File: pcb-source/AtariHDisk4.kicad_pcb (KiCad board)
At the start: 4 copper layers, 97.3 x 69.6 mm, 78 parts, among them J1 JTAG, J10 ST ACSI BUS, J14 MicroSD Card 0, J2 Program_enable, J3 SD Card 1, J4 UPDI, J5 Conn_01x02_Female, J6 Conn_02x03_Odd_Even, Q3 BC847, Q4 BC847, U1 74LVC245, U11 74LVC8T245, U2 MAX3232, U3 AZ1117-5.0, U4 Oscillator7x5, U5 MCP795xx, U7 AMS1117-3.3, U8 AMS1117-1.8, U9 5M80Z, Y1 32KHz

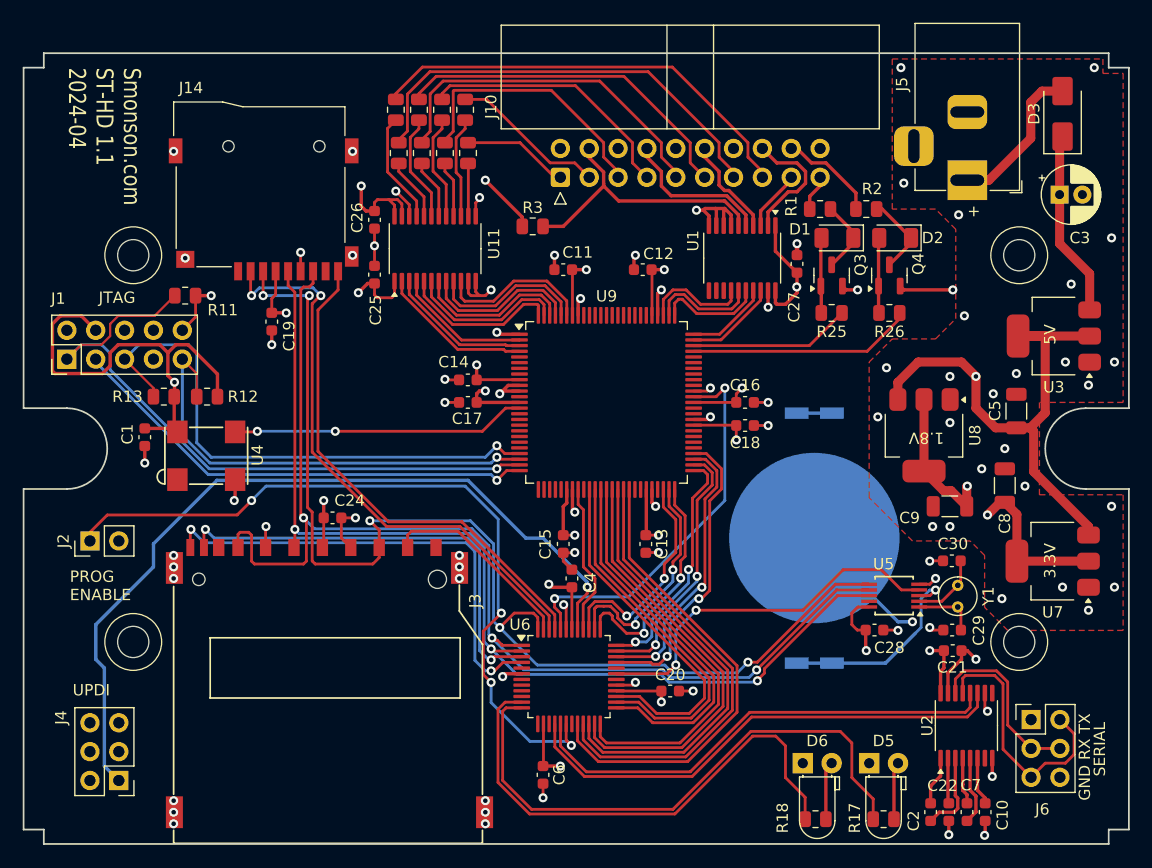
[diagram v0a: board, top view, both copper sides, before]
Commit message: STM32C01 version, now in a working state (#6)
Code for V2 board, proven and now working.
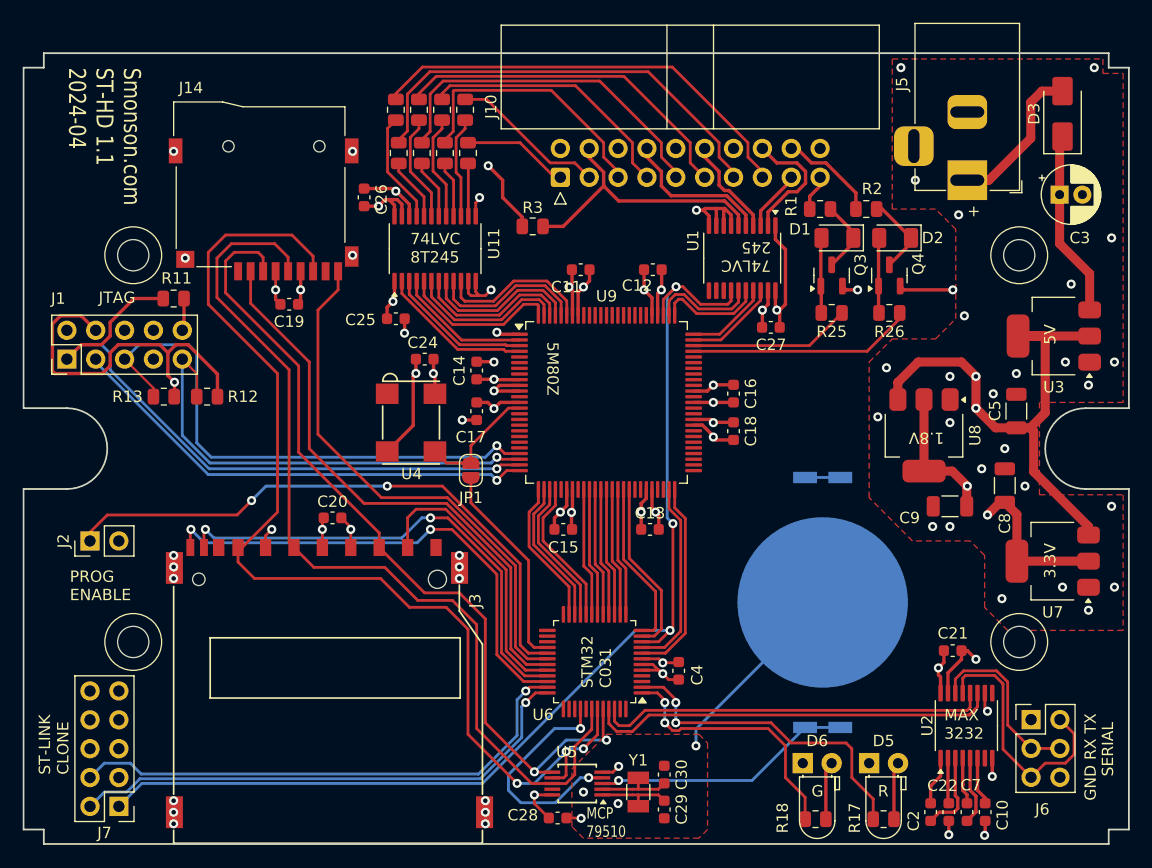
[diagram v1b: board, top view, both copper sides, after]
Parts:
- removed C1, C6: 0.1uF, Capacitor_SMD:C_0603_1608Metric
- removed J4: UPDI, Connector_PinHeader_2.54mm:PinHeader_2x03_P2.54mm_Vertical
- added J7: ST-LINK, Connector_PinHeader_2.54mm:PinHeader_2x05_P2.54mm_Vertical, F.Cu at (63.3, 125.5)
- added JP1: SolderJumper_2_Open, Jumper:SolderJumper-2_P1.3mm_Open_RoundedPad1.0x1.5mm, F.Cu at (94.2, 95.9)
- C21, C28: value C -> 0.1uF
- R17, R18: value 2K -> 220
- R25, R26: value R -> 1K
- U6: value ~ -> STM32C031CxT
- Y1: footprint Crystal:Crystal_C38-LF_D3.0mm_L8.0mm_Vertical -> simon:Crystal_SMD_ECX_31B-2Pin_3.2x1.5mm
- moved Y1 33.5 mm to (109.0, 124.2), turned to 90 degrees
- moved C20 33.4 mm to (82.1, 100.1)
- moved C28 32.4 mm to (101.9, 126.5)
- moved U5 32.4 mm to (103.6, 123.5)
- moved C30 31.5 mm to (111.3, 122.7), turned to 90 degrees
- moved C29 29.9 mm to (111.3, 125.7), turned to -90 degrees
- moved U4 18.0 mm to (88.8, 91.8), turned to 90 degrees
- moved C24 16.2 mm to (90.2, 86.1), turned to 180 degrees
- moved C4 12.4 mm to (112.5, 113.5)
- moved C27 6.04 mm to (120.6, 83.3), turned to 180 degrees
- moved BT1 5.71 mm to (125.2, 107.5)
- moved C25 4.31 mm to (87.6, 82.5), turned to 0 degrees
- moved U6 2.61 mm to (105.1, 112.7), turned to 180 degrees
- moved C26 2.18 mm to (84.8, 71.9), turned to 90 degrees
- moved C19 2.16 mm to (78.2, 81.3), turned to 0 degrees
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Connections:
- R17 pad 1: /ATMega/LED0 -> /Microcontroller/LED0
- R18 pad 1: /ATMega/LED1 -> /Microcontroller/LED1
- U2 pad 11: /ATMega/TX -> /Microcontroller/TX
- U2 pad 12: /ATMega/RX -> /Microcontroller/RX
- U5 pad 4: /ATMega/CLK_SS -> /Microcontroller/CLK_SS
- U6 pad 1: /MISO -> /Microcontroller/LED1
- U6 pad 10: unconnected-(U6-PC0-Pad10) -> /F_RESET
- U6 pad 11: /ATMega/LED1 -> /A_D0
- U6 pad 12: /ATMega/LED0 -> /A_D1
- U6 pad 13: unconnected-(U6-PC3-Pad13) -> /A_D2
- U6 pad 14: +3V3 -> /A_D3
- U6 pad 15: (no net) -> /A_D4
- U6 pad 16: /ATMega/TX -> /A_D5
- U6 pad 17: /ATMega/RX -> /A_D6
- U6 pad 18: Net-(J2-Pin_1) -> /A_D7
- U6 pad 19: unconnected-(U6-PC7-Pad19) -> /A_CS
- U6 pad 2: /SCK -> /Microcontroller/LED0
- U6 pad 20: /A_D0 -> /A_BUS_DIR
- U6 pad 21: /A_D1 -> /A_CMD
- U6 pad 22: /A_D2 -> /A_EXTRA2
- U6 pad 23: /A_D3 -> /A_EXTRA
- U6 pad 24: /A_D4 -> unconnected-(U6-PB12-Pad24)
- U6 pad 25: /A_D5 -> unconnected-(U6-PB13-Pad25)
- U6 pad 26: /A_D6 -> unconnected-(U6-PB14-Pad26)
- U6 pad 27: /A_D7 -> unconnected-(U6-PB15-Pad27)
- U6 pad 28: +3V3 -> /A_CLKOUT
- U6 pad 29: GND -> Net-(J2-Pin_1)
- U6 pad 3: /CARD1_DET -> unconnected-(U6-PC15-Pad3)
- U6 pad 30: unconnected-(U6-PE0-Pad30) -> /CARD0_DET
- U6 pad 31: /ATMega/CLK_SS -> /AVR_SS0
- U6 pad 32: unconnected-(U6-PE2-Pad32) -> /AVR_SS1
- U6 pad 33: /A_EXTRA2 -> /CARD1_DET
- U6 pad 34: /A_EXTRA -> /CARD1_WP
- U6 pad 35: /A_READY -> /Microcontroller/SWDIO
- U6 pad 36: /A_INT -> /Microcontroller/SWCLK
- U6 pad 37: /A_CMD -> unconnected-(U6-PA15-Pad37)
- U6 pad 38: /A_BUS_DIR -> unconnected-(U6-PD0-Pad38)
- U6 pad 39: /A_CS -> unconnected-(U6-PD1-Pad39)
- U6 pad 4: /CARD1_WP -> unconnected-(U6-PF3-Pad4)
- U6 pad 40: /A_RESET -> /Microcontroller/CLK_SS
- U6 pad 41: /ATMega/UPDI -> (no net)
- U6 pad 42: +3V3 -> /SCK
- U6 pad 43: GND -> /MISO
- U6 pad 44: /CLOCK8 -> /MOSI
- U6 pad 45: /CARD0_DET -> /Microcontroller/TX
- U6 pad 46: /AVR_SS0 -> /Microcontroller/RX
- U6 pad 47: /AVR_SS1 -> unconnected-(U6-PB8-Pad47)
- U6 pad 48: /MOSI -> unconnected-(U6-PB9-Pad48)
- U6 pad 5: unconnected-(U6-PB1-Pad5) -> +3V3
- U6 pad 6: GND -> +3V3
- U6 pad 7: unconnected-(U6-PB3-Pad7) -> GND
- U6 pad 8: unconnected-(U6-PB4-Pad8) -> /A_READY
- U6 pad 9: unconnected-(U6-PB5-Pad9) -> /A_INT
- U9 pad 26: unconnected-(U9-IO-Pad26) -> /A_EXTRA
- U9 pad 27: unconnected-(U9-IO-Pad27) -> /A_EXTRA2
- U9 pad 28: unconnected-(U9-IO-Pad28) -> /A_CMD
- U9 pad 29: unconnected-(U9-IO-Pad29) -> /A_BUS_DIR
- U9 pad 33: /A_RESET -> unconnected-(U9-IO-Pad33)
- U9 pad 34: unconnected-(U9-IO-Pad34) -> /A_CS
- U9 pad 48: /A_CS -> unconnected-(U9-IO-Pad48)
- U9 pad 49: /A_BUS_DIR -> /A_INT
- U9 pad 50: /A_CMD -> /A_READY
- U9 pad 51: /A_INT -> unconnected-(U9-IO-Pad51)
- U9 pad 52: /A_READY -> unconnected-(U9-IO-Pad52)
- U9 pad 53: /A_EXTRA -> unconnected-(U9-IO-Pad53)
- U9 pad 54: /A_EXTRA2 -> unconnected-(U9-IO-Pad54)
- U9 pad 64: /CLOCK8 -> unconnected-(U9-IO/CLK3-Pad64)
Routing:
- net +3V3: track 449.2 -> 109.1 mm, vias 17 -> 16
- net /F_RESET: track 9.27 -> 98.2 mm, vias 0 -> 3
- net /ATMega/UPDI: track 72.5 -> 0.00 mm, vias 1 -> 0
- net /ATMega/LED0: track 50.4 -> 0.00 mm
- net /Microcontroller/SWDIO: track 0.00 -> 46.2 mm, vias 0 -> 1
- net /Microcontroller/SWCLK: track 0.00 -> 46.0 mm, vias 0 -> 1
- net /ATMega/LED1: track 45.6 -> 0.00 mm
- net /ATMega/TX: track 44.0 -> 0.00 mm
- net /ATMega/RX: track 42.6 -> 0.00 mm
- net /Microcontroller/TX: track 0.00 -> 36.1 mm
- net /Microcontroller/RX: track 0.00 -> 34.5 mm
- net /CLOCK8: track 34.5 -> 0.00 mm, vias 2 -> 0
- net /ATMega/CLK_SS: track 33.0 -> 0.00 mm, vias 2 -> 0
- net /Microcontroller/LED0: track 0.00 -> 28.9 mm, vias 0 -> 2
- net /A_D2: track 38.9 -> 11.3 mm
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- added copper zone on In2.Cu, net +3V3
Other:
- board text added: "5M80Z"
- board text added: "74LVC 245"
- board text added: "74LVC 8T245"
- board text added: "CR2016"
- board text added: "G"
- board text added: "MAX 3232"
- board text added: "MCP 79510"
- board text added: "R"
- board text added: "ST-LINK CLONE"
- board text added: "STM32 C031"
- board text removed: "UPDI"

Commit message: 1.2 version with 2 SPI buses
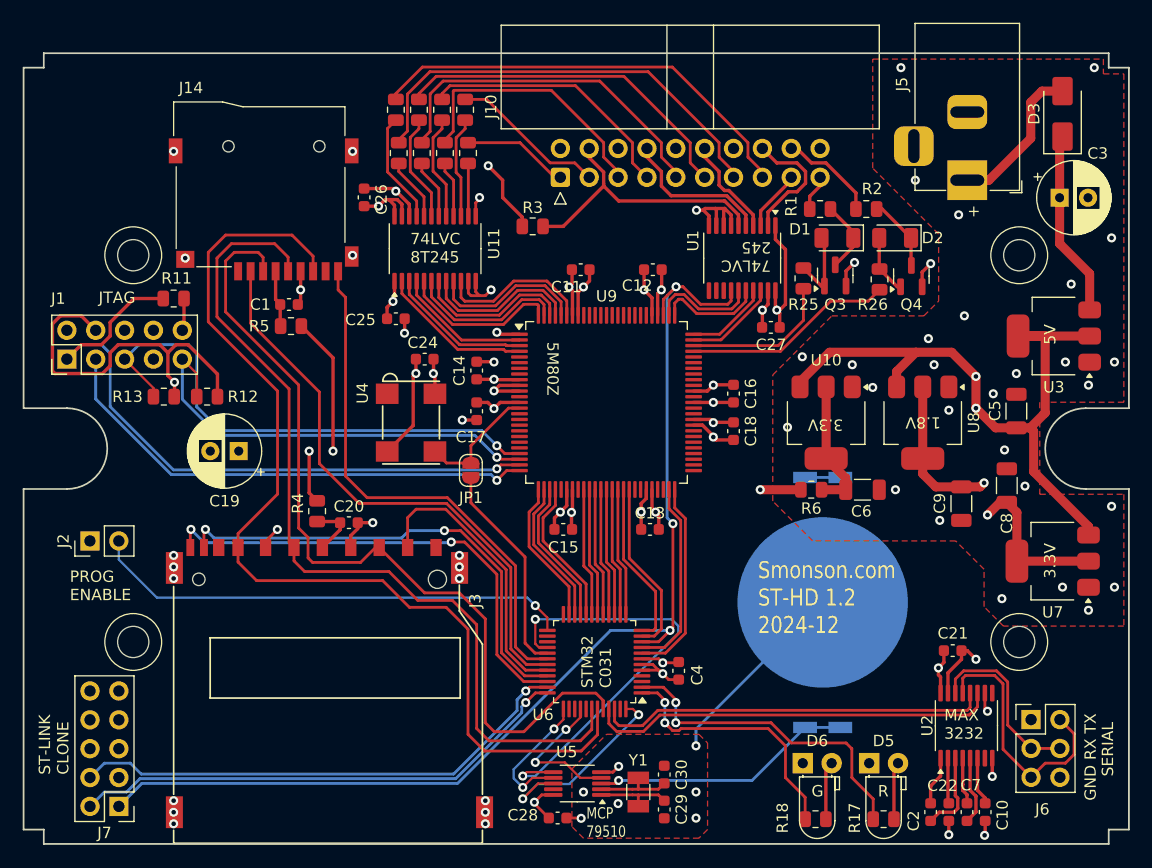
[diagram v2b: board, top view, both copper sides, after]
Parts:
- added C1: 0.1uF, Capacitor_SMD:C_0603_1608Metric, F.Cu at (78.2, 81.3)
- added C6: 4.7uF, Capacitor_SMD:C_1206_3216Metric, F.Cu at (128.7, 97.6)
- added R4: 5, Resistor_SMD:R_0805_2012Metric, F.Cu at (80.7, 99.5)
- added R5: 5, Resistor_SMD:R_0805_2012Metric, F.Cu at (78.4, 83.2)
- added R6: 10, Resistor_SMD:R_0805_2012Metric, F.Cu at (124.2, 97.6)
- added U10: AMS1117-3.3, Package_TO_SOT_SMD:SOT-223-3_TabPin2, F.Cu at (125.5, 91.7)
- C19: value 0.1uF -> 220uF; footprint Capacitor_SMD:C_0603_1608Metric -> Capacitor_THT:CP_Radial_D6.3mm_P2.50mm
- C3: footprint Capacitor_THT:CP_Radial_D5.0mm_P2.00mm -> Capacitor_THT:CP_Radial_D6.3mm_P2.50mm
- R17: value 220 -> 470
- R18: value 220 -> 2K
- moved C19 13.7 mm to (73.8, 94.2), turned to 180 degrees
- moved R25 3.93 mm to (123.5, 79.0), turned to 90 degrees
- moved R26 3.08 mm to (130.2, 79.1), turned to 90 degrees
- moved Q4 1.94 mm to (133.0, 78.8)
- moved C20 1.51 mm to (83.5, 100.5)
- moved U8 1.12 mm to (134.0, 91.7)
- moved C9 1.03 mm to (137.4, 98.8), turned to -90 degrees
- moved Q3 0.32 mm to (126.3, 78.7)
- moved C3 0.27 mm to (146.1, 71.9)
- moved C8 0.18 mm to (141.4, 97.2)
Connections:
- C19 pad 1: +3V3 -> +SD3V3
- C20 pad 1: +3V3 -> Net-(J3-VDD)
- J14 pad 4: +3V3 -> Net-(J14-VDD)
- J2 pad 1: Net-(J2-Pin_1) -> GND
- J2 pad 2: GND -> Net-(J2-Pin_2)
- J3 pad 4: +3V3 -> Net-(J3-VDD)
- U5 pad 6: /MOSI -> /RTC_MOSI
- U5 pad 7: /MISO -> /RTC_MISO
- U5 pad 8: /SCK -> /RTC_CLK
- U6 pad 25: unconnected-(U6-PB13-Pad25) -> Net-(J2-Pin_2)
- U6 pad 28: /A_CLKOUT -> /RTC_MOSI
- U6 pad 29: Net-(J2-Pin_1) -> /A_CLKOUT
- U6 pad 37: unconnected-(U6-PA15-Pad37) -> /RTC_MISO
- U6 pad 48: unconnected-(U6-PB9-Pad48) -> /RTC_CLK
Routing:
- net +SD3V3: track 0.00 -> 72.1 mm, vias 0 -> 3
- net Net-(J2-Pin_1): track 53.0 -> 0.00 mm, vias 2 -> 0
- net Net-(J2-Pin_2): track 0.00 -> 42.6 mm, vias 0 -> 1
- net /RTC_MOSI: track 0.00 -> 38.5 mm, vias 0 -> 2
- net +1V8: track 89.2 -> 67.6 mm
- net /RTC_CLK: track 0.00 -> 17.8 mm, vias 0 -> 2
- net +5V: track 136.0 -> 148.0 mm
- net /RTC_MISO: track 0.00 -> 12.0 mm, vias 0 -> 2
- net Net-(U10-VO): track 0.00 -> 11.9 mm
- net /Microcontroller/CLK_SS: track 20.8 -> 12.9 mm
- net +3V3: track 109.1 -> 102.7 mm, vias 16 -> 14
- net /MISO: track 96.0 -> 90.0 mm, vias 3 -> 0
- net Net-(J3-VDD): track 0.00 -> 5.32 mm
- net Net-(J14-VDD): track 0.00 -> 5.00 mm
- net /SCK: track 82.2 -> 78.3 mm
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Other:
- board text added: "Smonson.com ST-HD 1.2 2024-12"
- board text removed: "Smonson.com ST-HD 1.1 2024-04"
